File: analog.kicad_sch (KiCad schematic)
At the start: 50 parts, among them J10 Spare diff in, J9 Sensor harness, U8 ADS1115 (0x48), U9 ADS1115 (0x49)

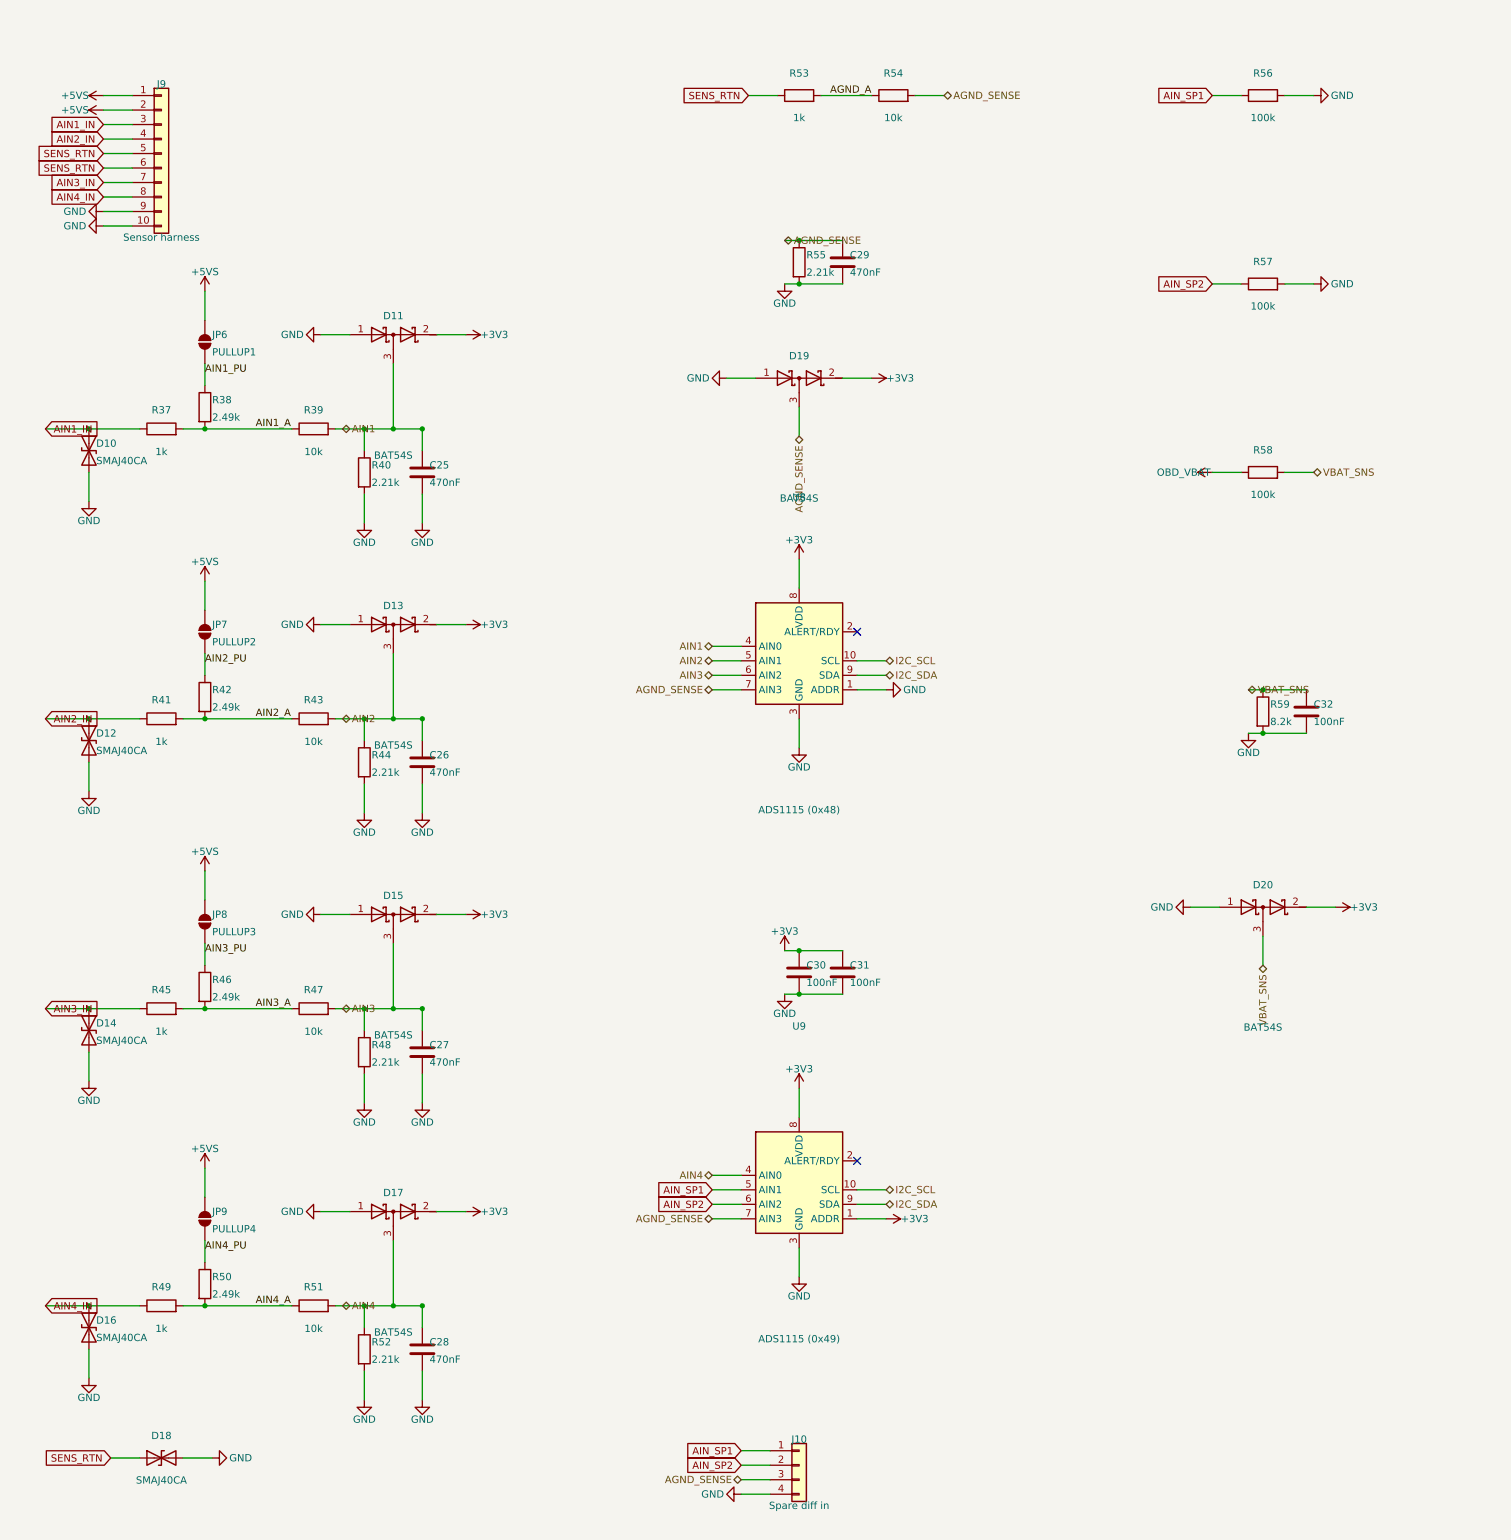
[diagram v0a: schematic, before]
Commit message: Schematic readability: fix the measurement, then fix the schematic
Three bugs in audit_schematic.py meant it was reporting clean on things
that were plainly wrong on the page:

  * lib_info() keyed its table on the NAME_1_1 unit sub-symbols while
    every placed symbol refers to the parent lib_id, so every lookup
    missed, every symbol came back with no pins, and the pin-number
    collisions the function exists to find were never once tested.

  * CHAR_W was an eyeballed 0.70. Plotting the sheets and measuring all
    1141 strings KiCad actually drew gives 0.851. Every string was
    modelled a sixth too narrow -- three characters' worth on a long net
    name.

  * A property's angle is stored RELATIVE to its symbol; KiCad adds the
    symbol's rotation before drawing. Reading the property angle alone
    modelled every field on every rotated part as a tall narrow box
    instead of a long flat one. That is how "SMAJ26CA" and "TERM" came
    to be printed through each other with the audit reporting zero.

Also replaced the "unwired" proxy. It asked whether a wire end lay
within 12 mm of a symbol's ORIGIN, which is fine for an 0603 and wrong
for everything bigger: the MCP2518FD, the microSD socket and both
SRV05-4s were reported floating while fully wired, and the mounting
holes were counted although they have no pins. It now builds the wire
graph and asks whether a symbol shares a conductor with another symbol.

With the measurement honest, the fixing half:

  * gen/tidy_sch_text.py (new), the schematic's tidy_silk.py. Nudges
    colliding references and values, slides a label along its own wire,
    and pulls the free end of a stub outward when a label needs room --
    taking the wire with it so nothing is disconnected. Bodies and
    junctions are obstacles as well as text, because clearing a value
    off a neighbour's value and onto that neighbour's symbol is not a
    fix. Iterates until it stops improving.

  * justify_for(). Block labels hardcoded "just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
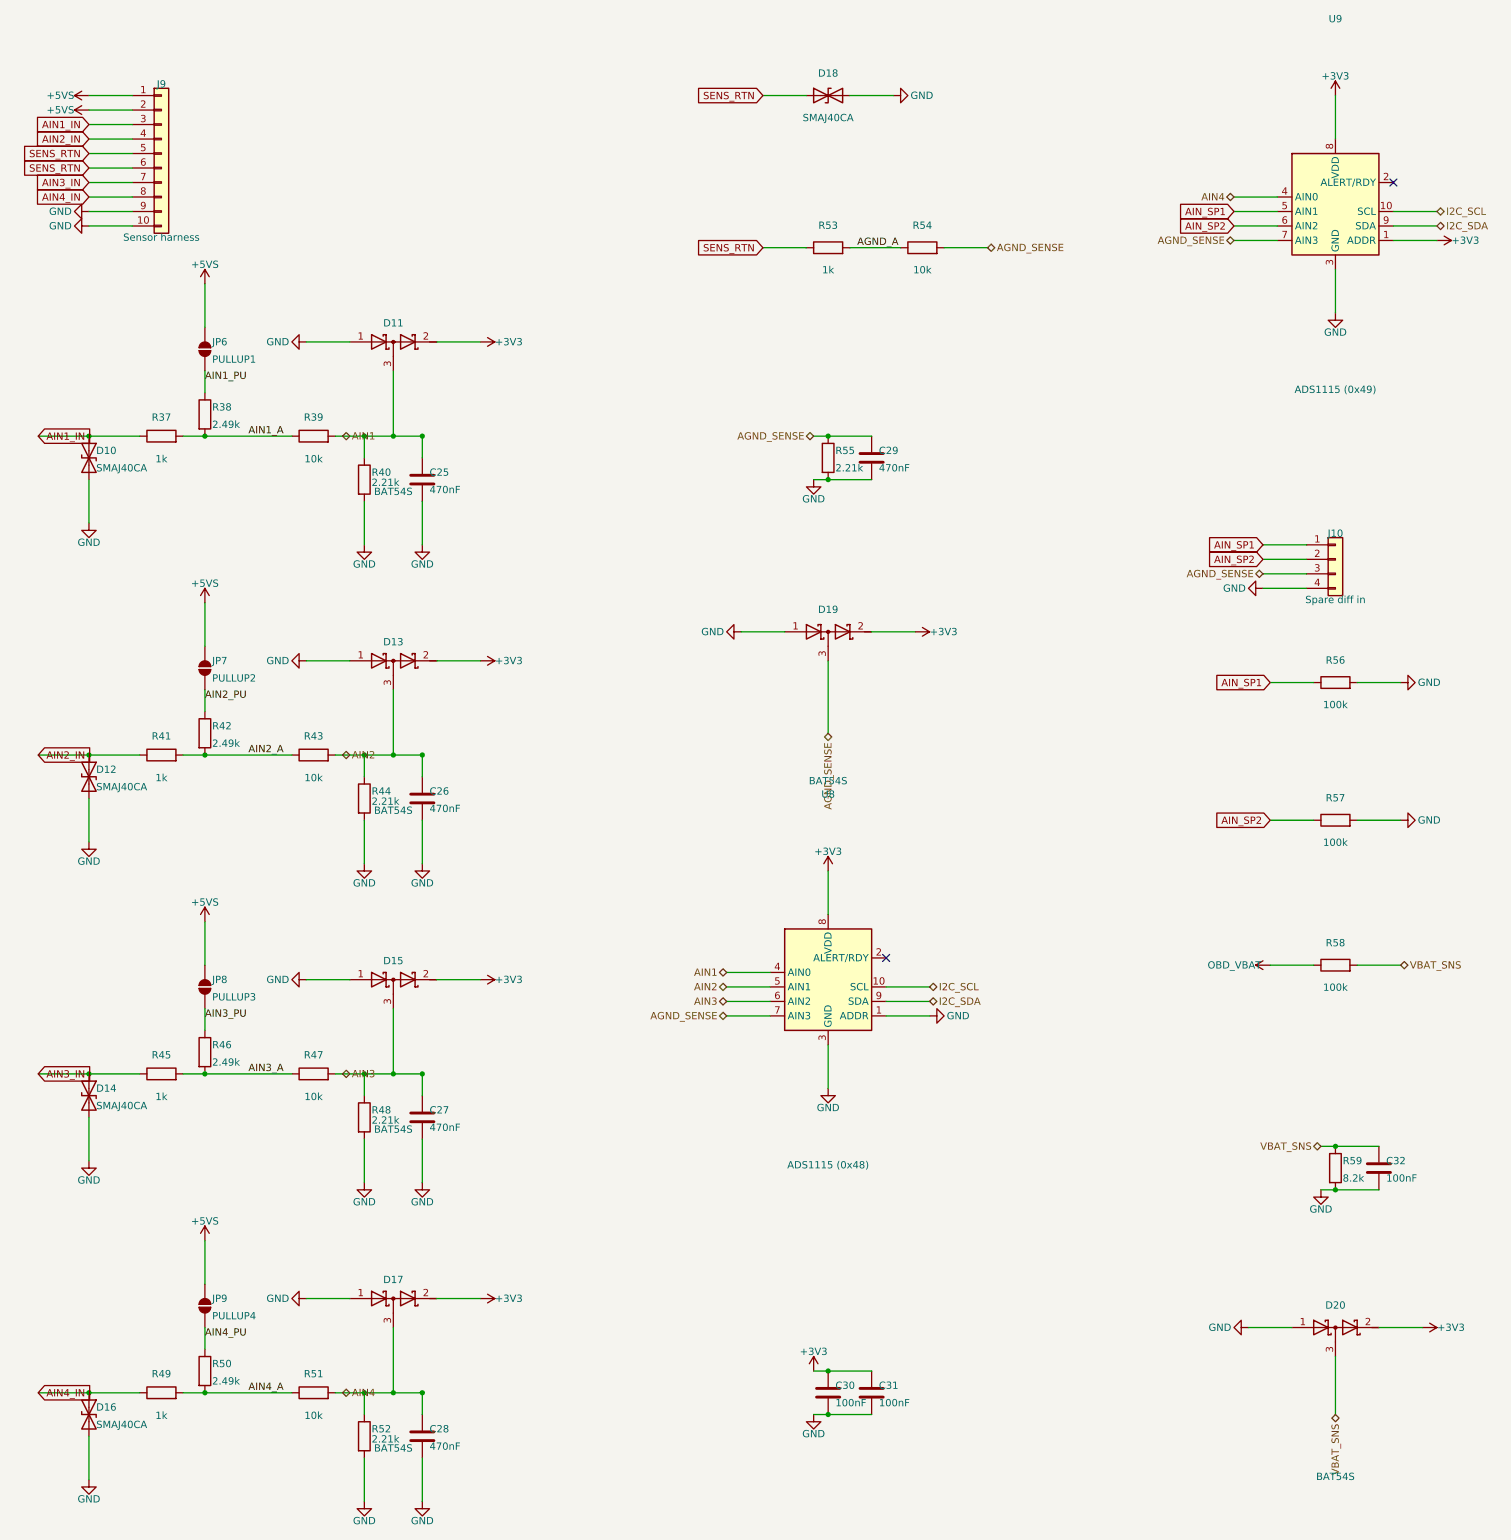
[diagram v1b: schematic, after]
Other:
- moved on the sheet: C25, C26, C27, C28, C29, C30, C31, C32, D10, D11, D12, D13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

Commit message: Draw the circuits that were only ever held together by net names
You wanted the hanging parts fixed. 48 of 160 symbols reached nothing
by wire -- a name at each end and nothing to follow. Now 7.

First the measurement, again. audit_schematic counted 59, and 11 of
those were decoupling capacitors with a rail symbol above and a ground
below, which is exactly how a person draws a decoupling capacitor. A
pin ending on a power symbol is DRAWN, not named; only a bare net label
makes the reader do the join in their head. Counting the two the same
made the number useless, so power symbols now count as a connection.

Seven new hand-drawn blocks, and the second CAN channel is no longer a
special case:

  can_bus()   the CAN block became a function and is instantiated
              twice. The whole second channel -- transceiver, choke,
              split termination -- was shelf-packed because it arrived
              after the block was written. Twenty parts on that sheet.
  MCP2518     the SPI CAN controller, crystal and load caps
  AUXSEL      the jumpers choosing CAN2 or K-line, clamps after them
  KLINE       the K-line driver, gate to drain to bus to receiver
  PWRIN       the loom, polyfuse, clamp and decoupler
  ADSPAIR     both ADCs and the I2C bus between them
  VBATSENSE   the battery divider, filter and clamp
  SENSERTN    the sensor return, drawn as a fifth channel because that
              is what differential ground makes it
  SCAPCHG     the supercap charge resistor and its bypass Schottky

Plus the SD block, which drew the terminators and the card but never
joined them: three card lines and the detect pull-up now run through.

Blocks can set their anchor's rotation. It used to keep whatever the
packer gave it, so every wire drawn to an anchor pin was betting on
that default -- the harness came out at 0 instead of 180 and put its
pins on the far side of the symbol from the waiting wire.

What is left is 5 fan-out connectors -- the two 22-way sockets, the
sens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
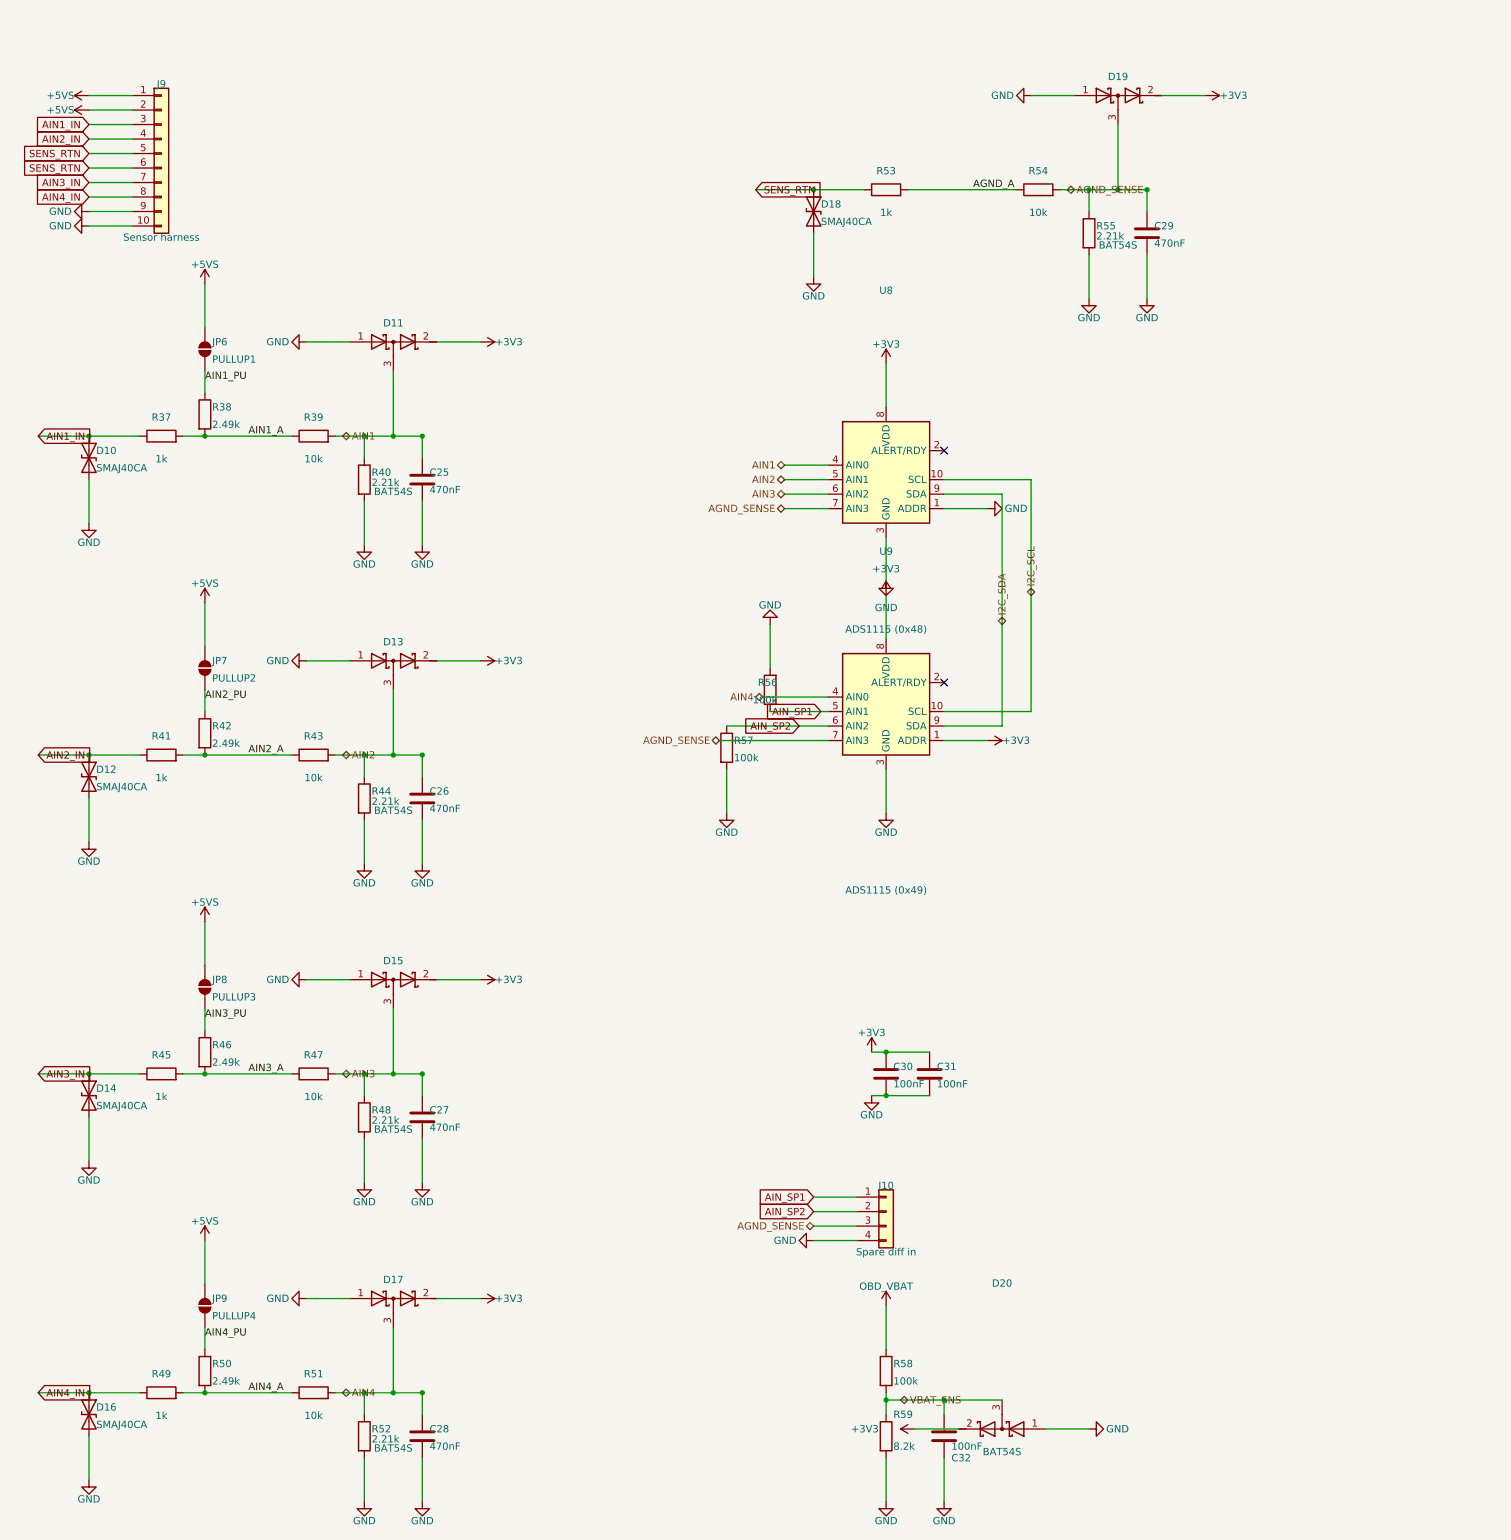
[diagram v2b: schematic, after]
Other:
- moved on the sheet: C29, C30, C31, C32, D18, D19, D20, J10, R53, R54, R55, R56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
